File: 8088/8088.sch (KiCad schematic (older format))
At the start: 116 parts, among them CON1 BARREL_JACK, P1 U3PA, P10 CONN_01X15, P11 CONN_01X05, P12 CONN_01X05, P13 CONN_01X08, P14 CONN_01X08, P3 U3PB, P4 RX/TX, P5 U4PC, P6 U4PA, P7 U4PB, P8 GND, P9 CONN_01X06, SW1 STEP_CLK, SW2 RESET, SW3 PWR, U1 8284, U10 2114, U11 ULN2803ADWR, U12 74LS14, U13 ULN2803ADWR, U14 ULN2803ADWR, U15 ULN2803ADWR, U16 LM1084IT-5.0/NOPB, U2 8088, U3 8755A, U4 8155, U5 8251A, U6 74LS32, U7 74LS138, U8 8282, U9 2114, Y1 12MHz

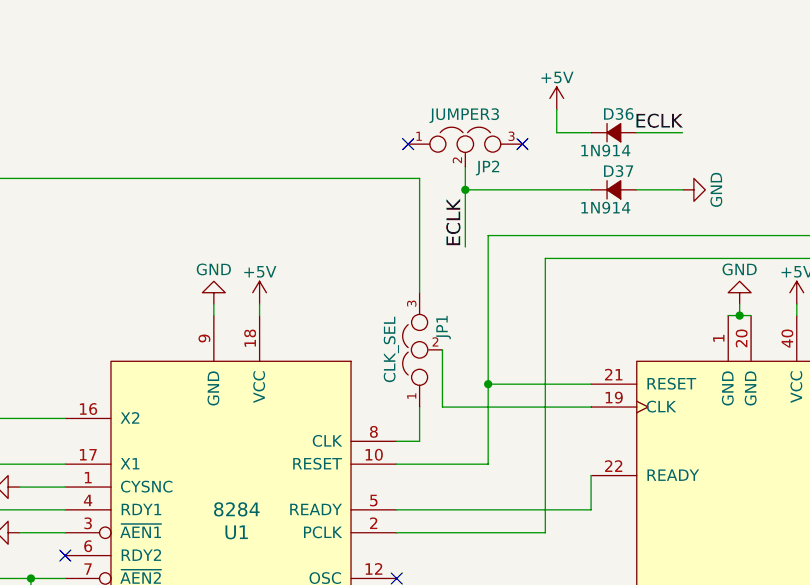
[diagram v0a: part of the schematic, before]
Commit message: Updated PCB to use top side power plane
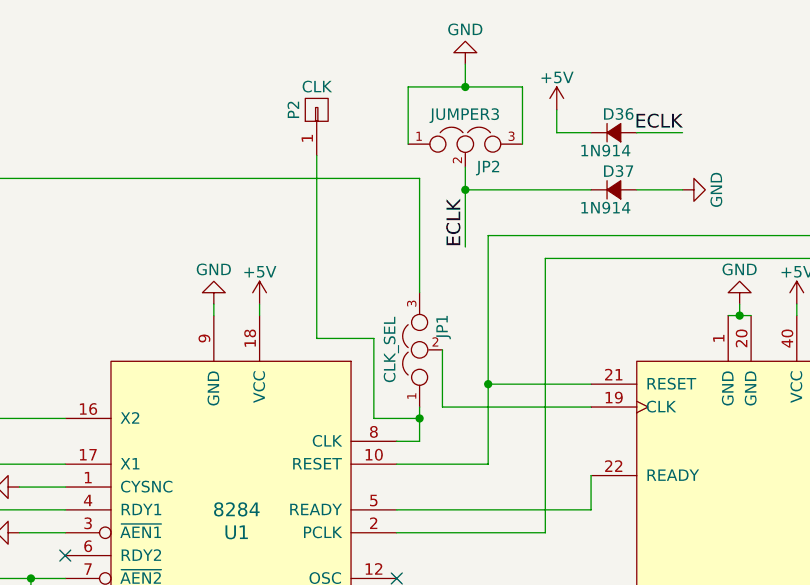
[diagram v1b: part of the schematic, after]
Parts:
- added P2: CLK, symbol CONN_01X01
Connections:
- net GND: now also JP2.1, JP2.3
- net at JP1.1, U1.8 (CLK): now also P2.1 (P1)
- no-connect marks 14 -> 12

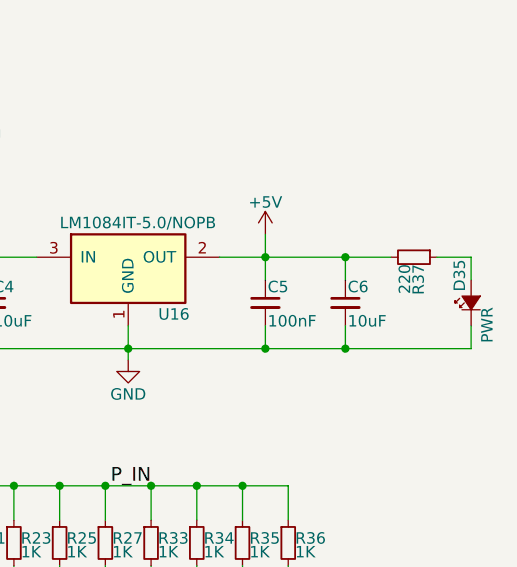
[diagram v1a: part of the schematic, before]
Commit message: Board revised based on prototype
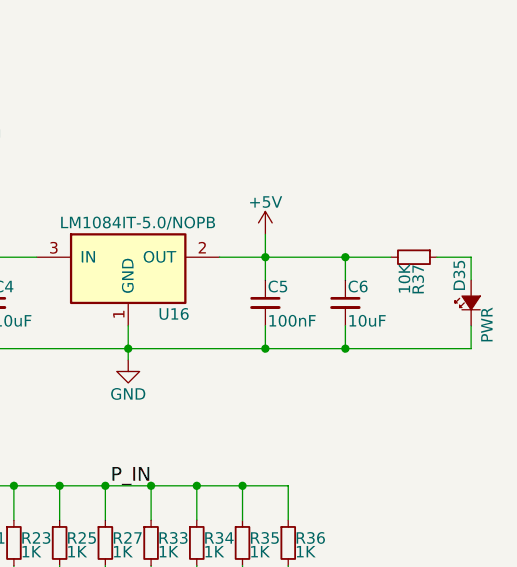
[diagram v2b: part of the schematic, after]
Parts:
- R37: value 220 -> 10K
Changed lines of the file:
@@
 P 20550 7600
 F 0 "R37" H 20580 7620 50  0000 L CNN
-F 1 "220" H 20580 7560 50  0000 L CNN
+F 1 "10K" H 20580 7560 50  0000 L CNN
 F 2 "Resistors_SMD:R_0805_HandSoldering" H 20550 7600 50  0001 C CNN
 F 3 "" H 20550 7600 50  0000 C CNN

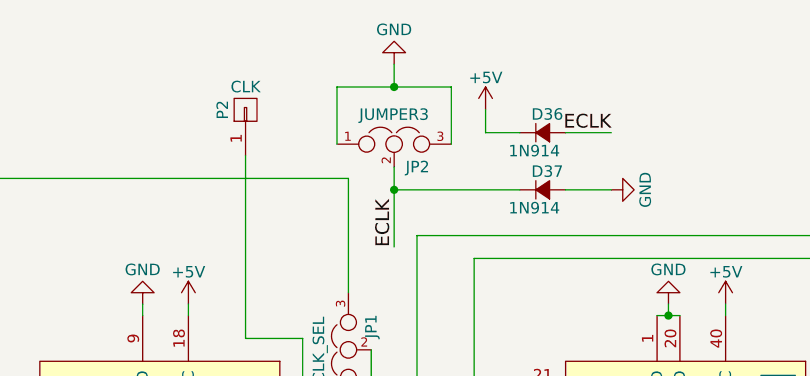
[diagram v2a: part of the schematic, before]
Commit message: Fixed issue with ECLK
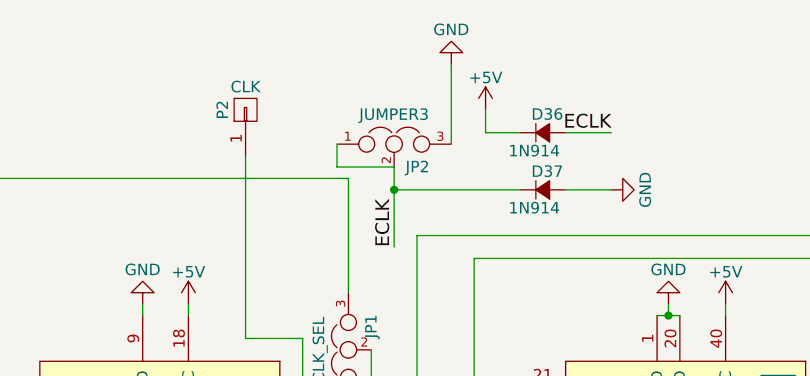
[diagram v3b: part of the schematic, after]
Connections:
- net ECLK: now also JP2.1
- net GND: no longer JP2.1
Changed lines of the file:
@@
 L GND #PWR?
 U 1 1 59E86756
-P 4450 3700
-F 0 "#PWR?" H 4450 3450 50  0001 C CNN
-F 1 "GND" H 4450 3550 50  0000 C CNN
-F 2 "" H 4450 3700 50  0000 C CNN
-F 3 "" H 4450 3700 50  0000 C CNN
-	1    4450 3700
+P 4700 3700
+F 0 "#PWR?" H 4700 3450 50  0001 C CNN
+F 1 "GND" H 4700 3550 50  0000 C CNN
+F 2 "" H 4700 3700 50  0000 C CNN
+F 3 "" H 4700 3700 50  0000 C CNN
+	1    4700 3700
 	-1   0    0    1
 $EndComp
 Wire Wire Line
-	4200 4050 4200 3800
+	4700 3700 4700 4050
 Wire Wire Line
-	4200 3800 4700 3800
+	4200 4050 4200 4150
 Wire Wire Line
-	4700 3800 4700 4050
-Wire Wire Line
-	4450 3700 4450 3800
-Connection ~ 4450 3800
+	4200 4150 4450 4150
 $EndSCHEMATC

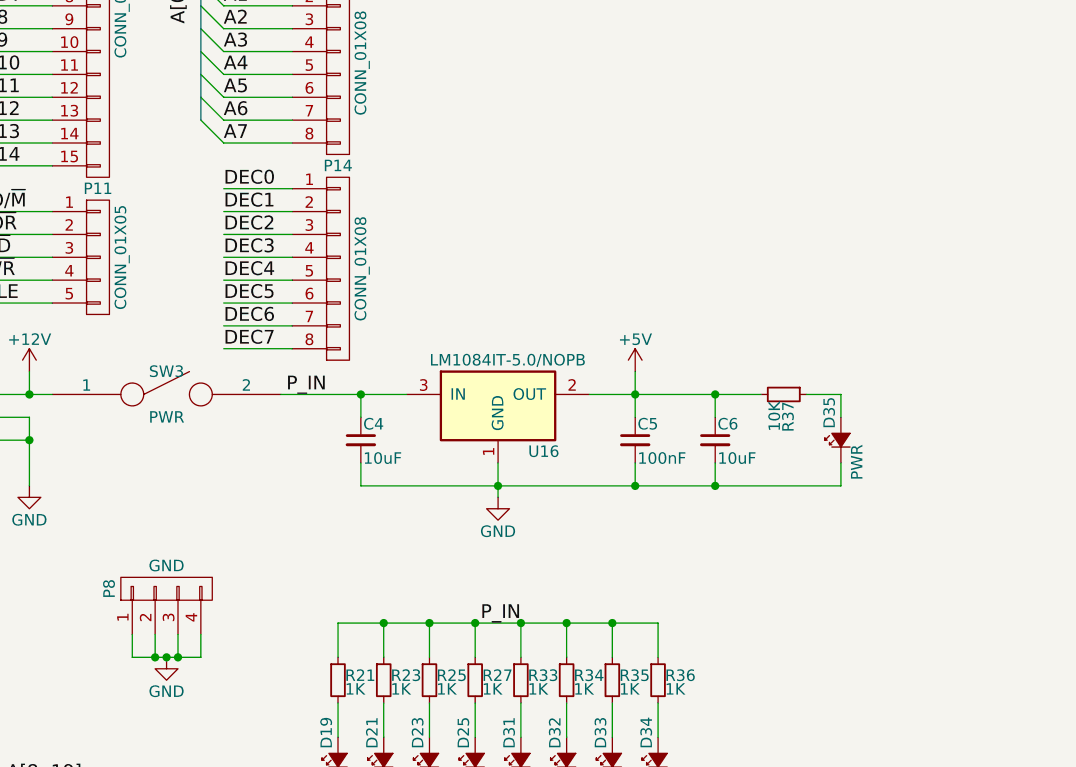
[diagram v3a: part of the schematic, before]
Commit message: Board rev2 done. Added buck converter circuit
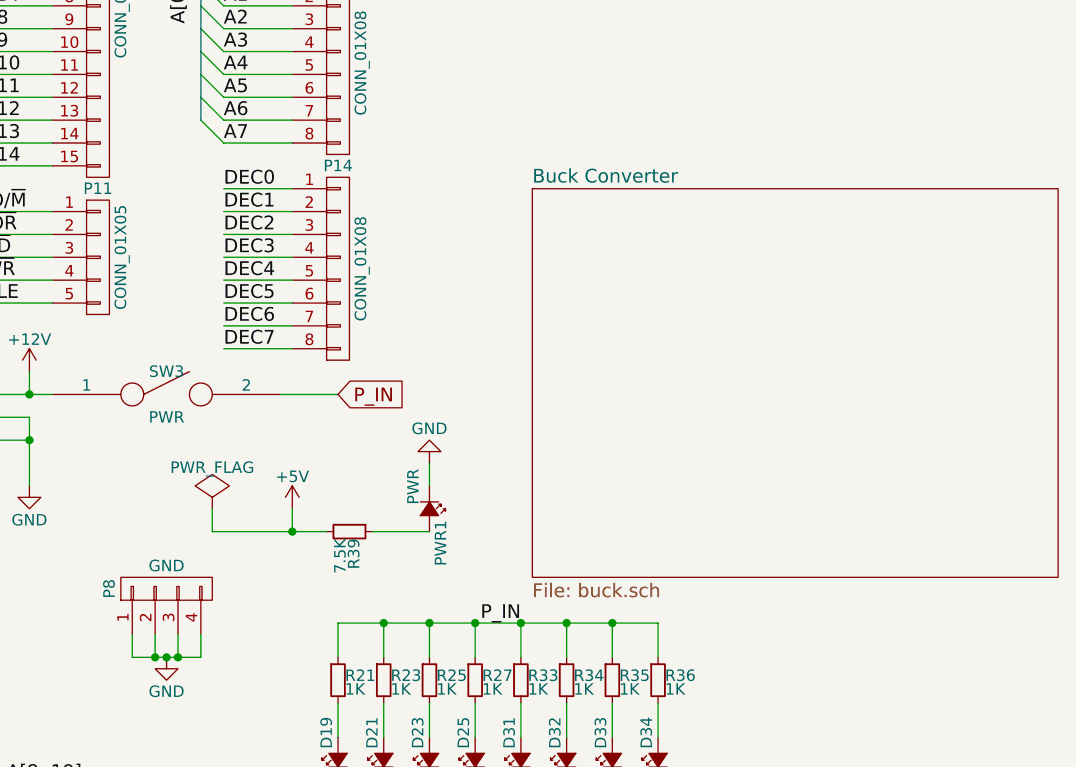
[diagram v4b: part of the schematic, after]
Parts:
- removed C4, C6: 10uF, Capacitors_SMD:C_0805_HandSoldering, symbol C_Small
- removed C5: 100nF, Capacitors_SMD:C_0805_HandSoldering, symbol C_Small
- removed D35: PWR, LEDs:LED_1206_HandSoldering, symbol Led_Small
- removed R37: 10K, Resistors_SMD:R_0805_HandSoldering, symbol R_Small
- removed U16: LM1084IT-5.0/NOPB, TO_SOT_Packages_SMD:TO-263-3_TabPin2, symbol LM1084IT-5.0/NOPB
- added PWR1: PWR, LEDs:LED_1206_HandSoldering, symbol Led_Small
- added R39: 7.5K, Resistors_SMD:R_0805_HandSoldering, symbol R_Small
- P2: footprint (none) -> Pin_Headers:Pin_Header_Straight_1x01_Pitch2.54mm
- SW1, SW2: footprint Library:PB2PIN -> Buttons_Switches_ThroughHole:SW_PUSH_6mm_h5mm
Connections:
- net +5V: now also R39.2
- net GND: now also PWR1.1 (K)
- new net: PWR1.2 (A), R39.1
